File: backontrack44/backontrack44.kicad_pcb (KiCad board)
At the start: 2 copper layers, 153.7 x 95.6 mm, 98 parts, among them J1 AudioJack4, J2 OLED, SW1-1 choc_SW_HS, SW1-2 choc_SW_HS, SW1-3 choc_SW_HS, SW1-4 choc_SW_HS, SW1-5 choc_SW_HS, SW1-6 choc_SW_HS, SW2-1 choc_SW_HS, SW2-2 choc_SW_HS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

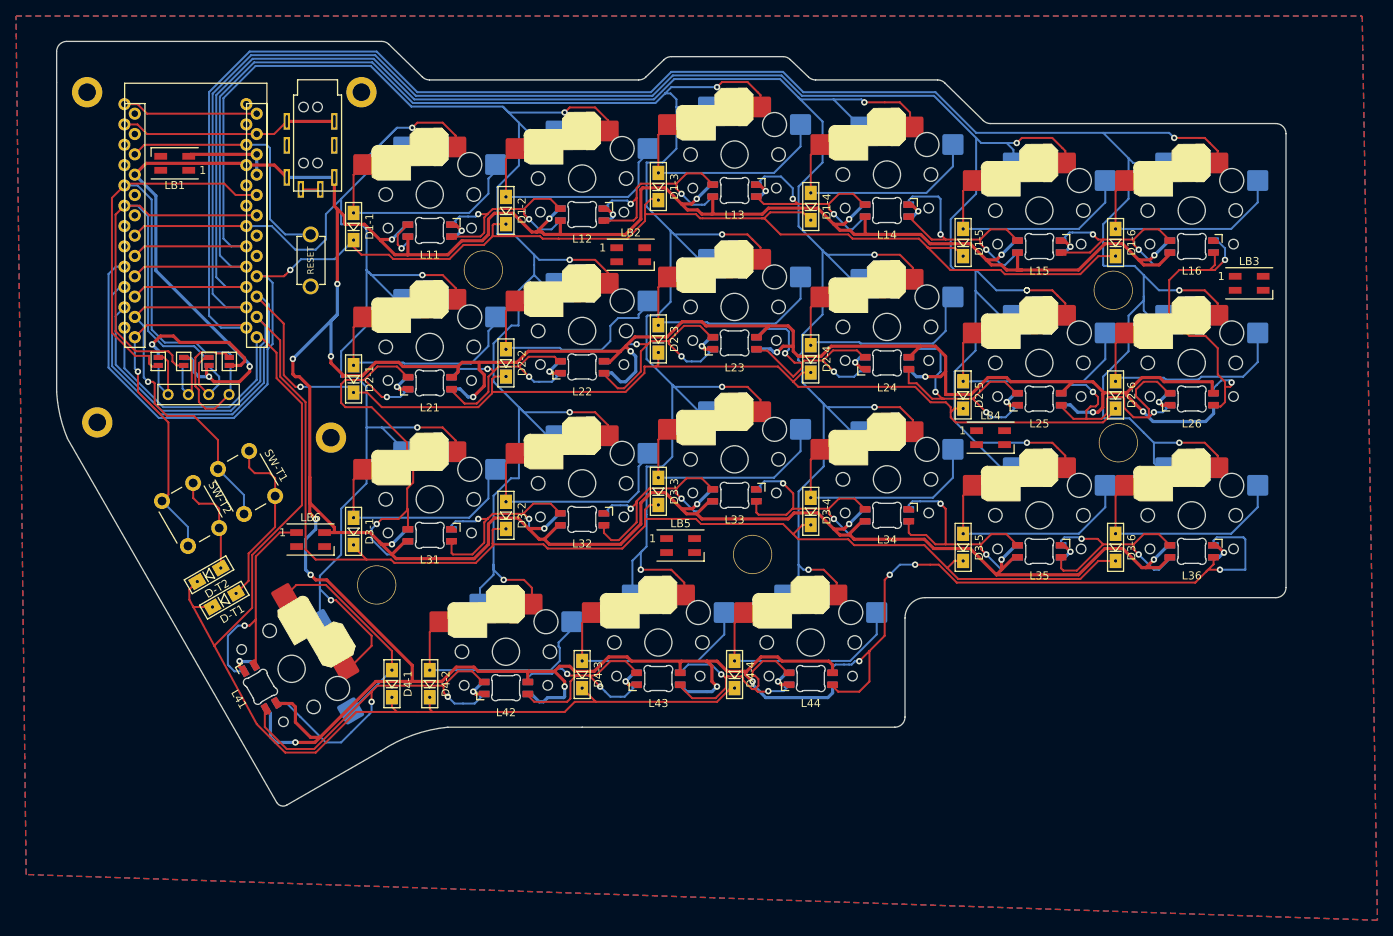
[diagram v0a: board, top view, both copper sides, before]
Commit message: added B-leds to back side as well
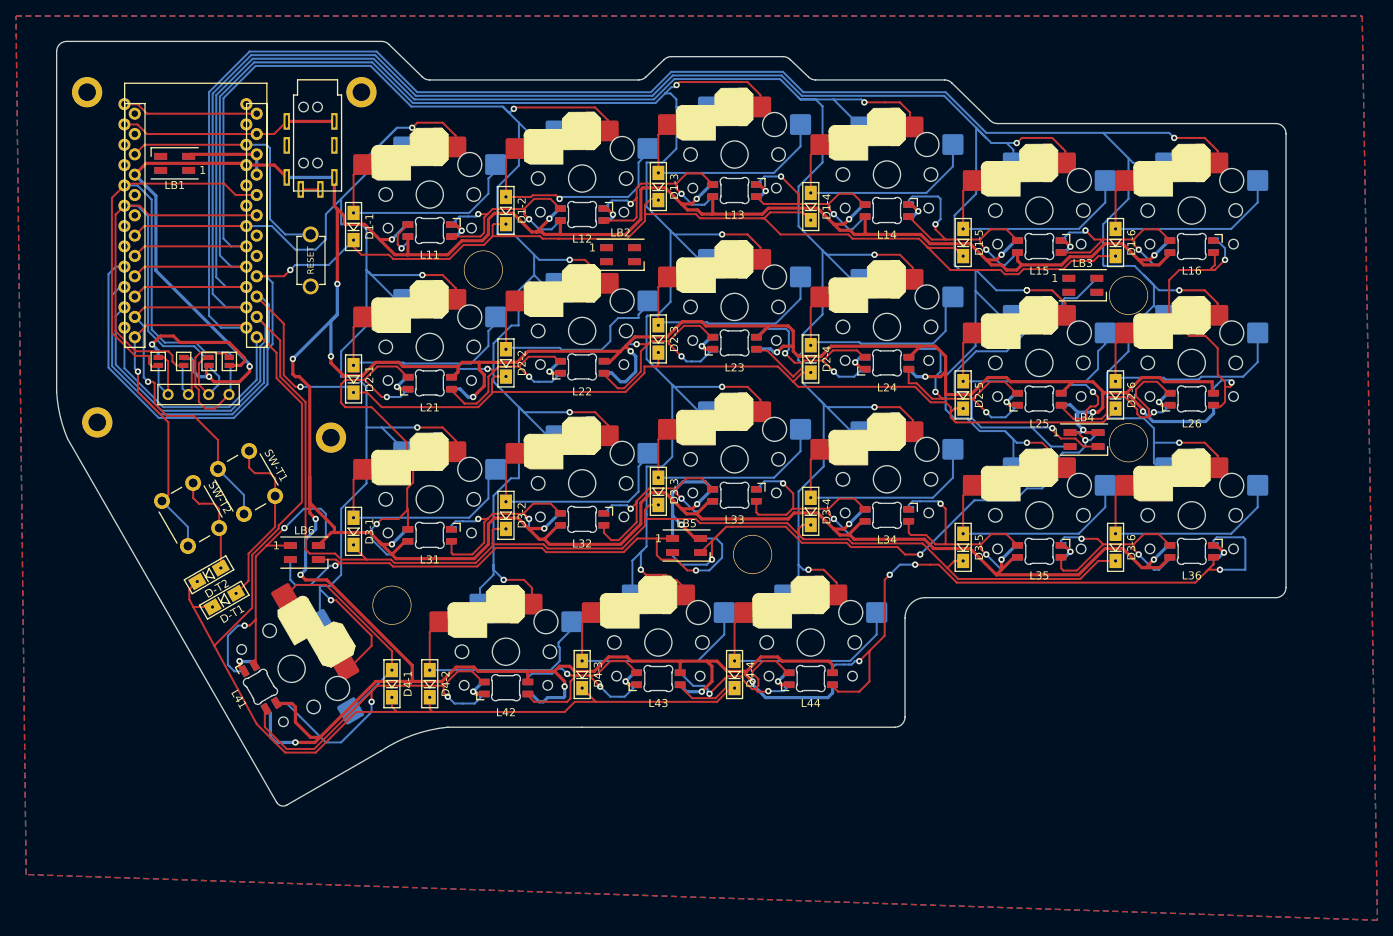
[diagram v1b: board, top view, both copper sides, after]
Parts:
- moved LB3 20.8 mm to (176.5, 53.3)
- moved LB4 11.7 mm to (176.7, 72.6)
- moved H5 3.17 mm to (90.2, 93.3)
- moved H6 2.01 mm to (182.2, 54.6)
- moved LB6 1.81 mm to (79.2, 86.8)
- moved H7 1.27 mm to (182.2, 73.0)
- moved LB2 1.27 mm to (118.7, 49.5)
- moved LB5 0.75 mm to (127.0, 85.9)
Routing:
- net Net-(LB5-Pad1): track 0.00 -> 73.0 mm, vias 0 -> 2
- net Net-(LB4-Pad1): track 0.00 -> 73.0 mm, vias 0 -> 3
- net Net-(LB3-Pad1): track 0.00 -> 54.9 mm, vias 0 -> 1
- net VCC: track 801.4 -> 825.4 mm, vias 29 -> 31
- net bigled-out: track 30.5 -> 42.9 mm, vias 1 -> 2
- net col6: track 303.0 -> 301.8 mm
- net col5: track 282.4 -> 283.5 mm
- net Net-(L43-Pad2): track 32.9 -> 33.8 mm
- net col4: track 258.6 -> 259.3 mm
- net col2: track 211.3 -> 210.5 mm
- net col1: track 176.1 -> 176.8 mm
- net row3: track 193.4 -> 194.1 mm
- net Net-(L14-Pad3): track 33.1 -> 33.6 mm
- net Net-(D1-2-Pad2): track 28.9 -> 29.3 mm, vias 0 -> 1
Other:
- outline, holes or cut-outs redrawn

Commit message: added missing "true" connections
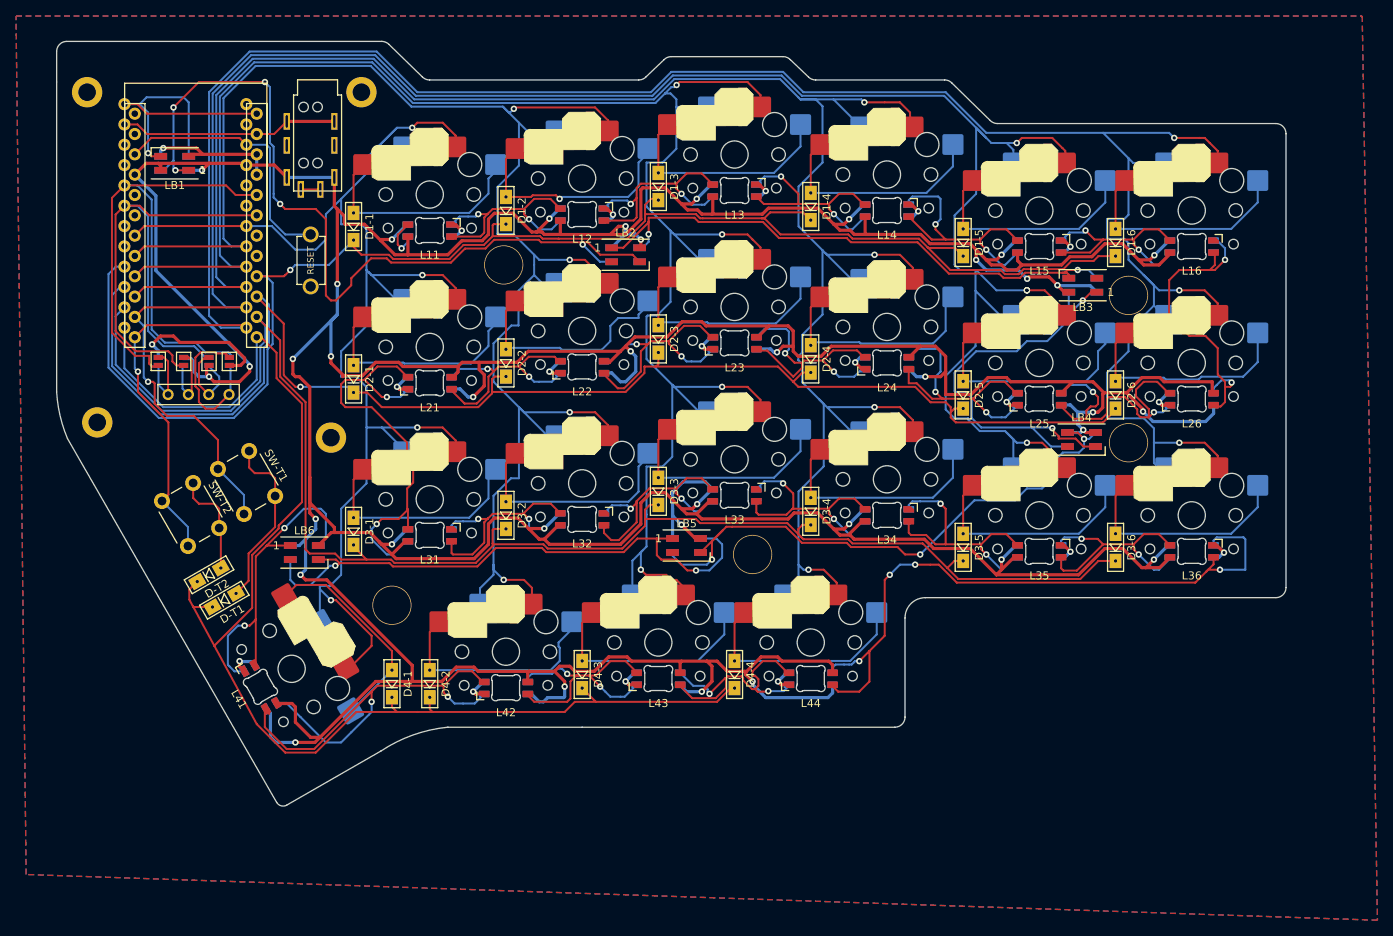
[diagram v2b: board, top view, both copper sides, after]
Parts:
- moved H8 2.62 mm to (104.1, 50.8)
- moved LB2 0.63 mm to (119.4, 49.5)
- moved LB4 0.31 mm to (176.4, 72.6)
- turned LB3 to 180 degrees
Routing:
- net Net-(LB1-Pad1): track 0.00 -> 106.0 mm, vias 0 -> 5
- net Net-(LB2-Pad1): track 0.00 -> 71.8 mm, vias 0 -> 2
- net VCC: track 825.4 -> 860.6 mm, vias 31 -> 37
- net LED: track 18.9 -> 40.7 mm, vias 0 -> 1
- net GND: track 83.8 -> 90.3 mm, vias 18 -> 19
- net Net-(LB3-Pad1): track 54.9 -> 56.2 mm, vias 1 -> 2
- net RESET: track 32.3 -> 33.0 mm
- net col5: track 283.5 -> 283.0 mm

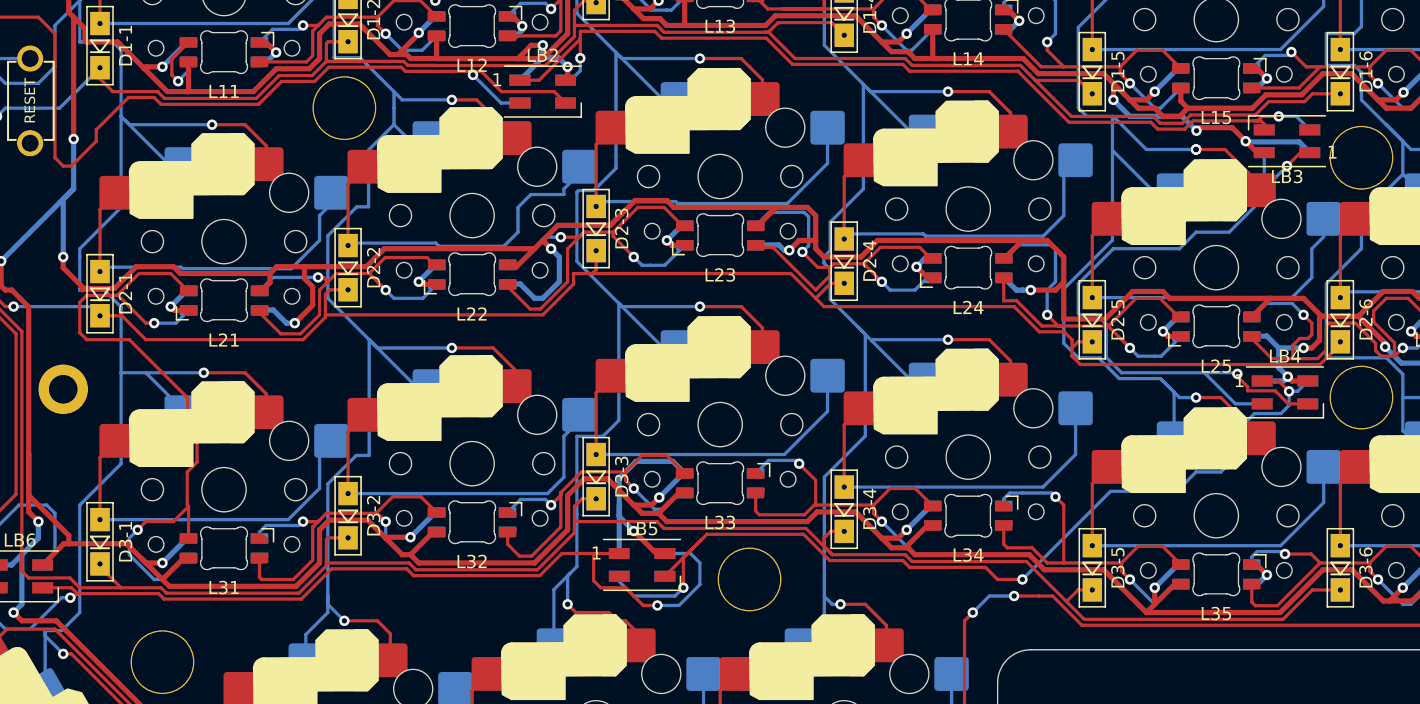
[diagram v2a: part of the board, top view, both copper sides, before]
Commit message: fixed some missing GND connections
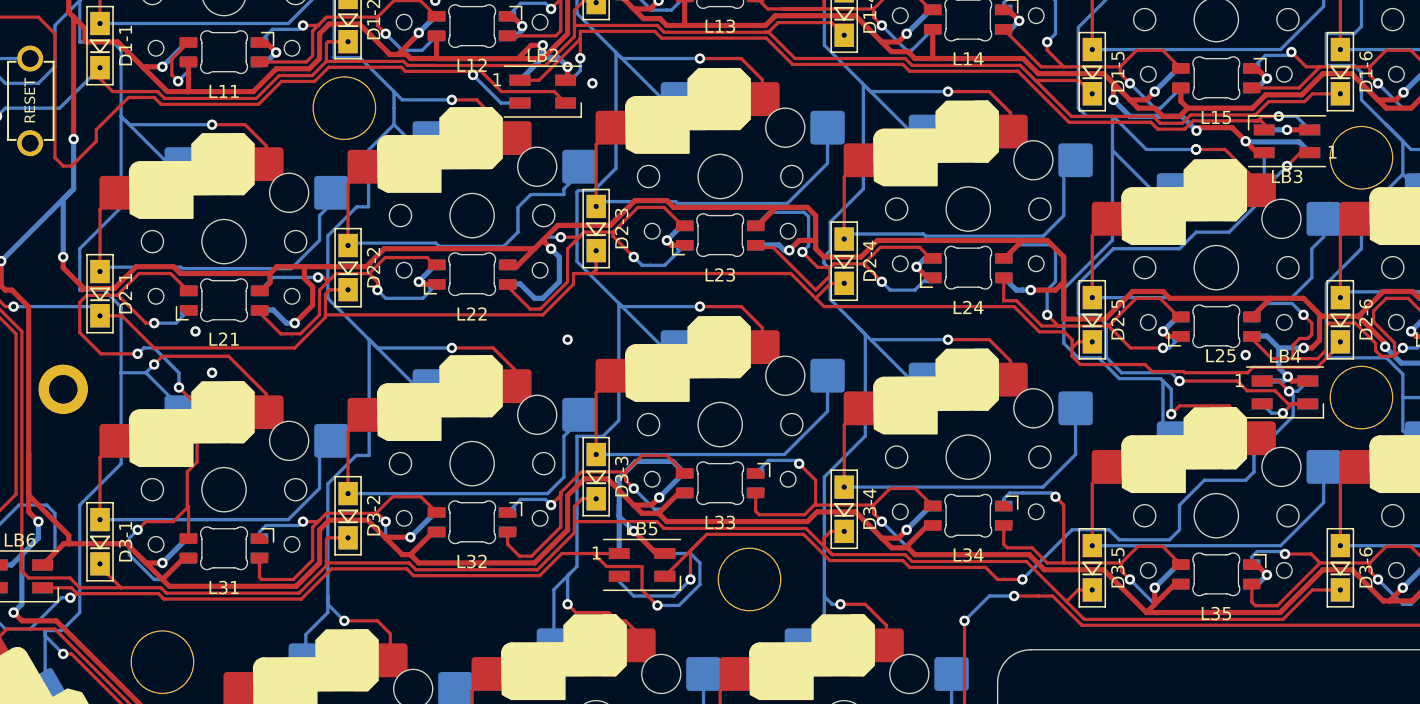
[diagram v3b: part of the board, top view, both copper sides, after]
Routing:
- net Net-(LB4-Pad1): track 72.9 -> 75.2 mm
- net col5: track 283.0 -> 284.6 mm
- net Net-(LB3-Pad1): track 56.2 -> 54.6 mm, vias 2 -> 3
- net Net-(L21-Pad3): track 53.7 -> 54.8 mm, vias 2 -> 4
- net row2: track 179.7 -> 180.8 mm
- net col1: track 176.8 -> 177.9 mm
- net Net-(L24-Pad2): track 36.0 -> 35.4 mm
- net GND: track 90.3 -> 90.5 mm, vias 19 -> 24
